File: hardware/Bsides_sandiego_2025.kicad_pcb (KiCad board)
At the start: 2 copper layers, 49.9 x 49.1 mm, 24 parts, among them J1 Conn_02x03_Odd_Even, SW1 RESET, SW2 SW_SPDT, U1 CH32V003FxPx

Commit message: feat(Hw):Update_PCB_And_Floorplan
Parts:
- added C3: 0.1uF, Capacitor_SMD:C_0603_1608Metric, F.Cu at (110.1, 115.6)
- added C4: 0.1uF, Capacitor_SMD:C_0603_1608Metric, F.Cu at (148.2, 115.8)
- added C5: 0.1uF, Capacitor_SMD:C_0603_1608Metric, F.Cu at (122.7, 115.6)
- added C6: 0.1uF, Capacitor_SMD:C_0603_1608Metric, F.Cu at (135.6, 115.7)
- added J2: OLED, Footprints:Display OLED 128 x32, F.Cu at (107.5, 100.1)
- added SW3: ~, Button_Switch_SMD:SW_SPST_TL3342, F.Cu at (105.1, 115.7)
- added SW4: ~, Button_Switch_SMD:SW_SPST_TL3342, F.Cu at (143.2, 115.8)
- added SW5: ~, Button_Switch_SMD:SW_SPST_TL3342, F.Cu at (117.7, 115.5)
- added SW6: ~, Button_Switch_SMD:SW_SPST_TL3342, F.Cu at (130.6, 115.7)
- moved R4 32.2 mm to (146.4, 77.6), turned to -90 degrees
- moved C2 25.5 mm to (105.3, 95.1), turned to 0 degrees
- moved R3 22.1 mm to (123.3, 60.5), turned to -90 degrees
- moved R6 19.5 mm to (116.9, 93.5)
- moved R7 17.2 mm to (135.2, 93.2)
- moved R1 14.3 mm to (113.5, 63.6), turned to 90 degrees
- moved R2 12.9 mm to (119.6, 67.5)
- moved R5 8.95 mm to (108.0, 77.6), turned to -90 degrees
- moved R8 5.18 mm to (131.8, 78.7)
- moved SW1 2.96 mm to (105.3, 91.4)
- moved C1 0.50 mm to (126.7, 83.2)
- turned D3 to -90 degrees
- turned D5 to -173.5 degrees
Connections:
- D1 pad 2: unconnected-(D1-A-Pad2) -> /LED1
- D2 pad 2: unconnected-(D2-A-Pad2) -> /LED2
- D3 pad 2: unconnected-(D3-A-Pad2) -> /LED3
- D4 pad 2: unconnected-(D4-A-Pad2) -> /LED4
- D5 pad 2: unconnected-(D5-A-Pad2) -> /LED5
- D6 pad 2: unconnected-(D6-A-Pad2) -> /LED6
- D7 pad 2: unconnected-(D7-A-Pad2) -> /LED7
- D8 pad 2: unconnected-(D8-A-Pad2) -> /LED8
- U1 pad 1: unconnected-(U1-PD4-Pad1) -> /LED1
- U1 pad 10: unconnected-(U1-PC0-Pad10) -> /LED7
- U1 pad 13: unconnected-(U1-PC3-Pad13) -> /LED8
- U1 pad 14: unconnected-(U1-PC4-Pad14) -> /LEFT
- U1 pad 15: unconnected-(U1-PC5-Pad15) -> /UP
- U1 pad 19: unconnected-(U1-PD2-Pad19) -> /DOWN
- U1 pad 2: unconnected-(U1-PD5-Pad2) -> /LED2
- U1 pad 20: unconnected-(U1-PD3-Pad20) -> /RIGHT
- U1 pad 3: unconnected-(U1-PD6-Pad3) -> /LED3
- U1 pad 5: unconnected-(U1-PA1-Pad5) -> /LED4
- U1 pad 6: unconnected-(U1-PA2-Pad6) -> /LED5
- U1 pad 8: unconnected-(U1-PD0-Pad8) -> /LED6
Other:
- board size 49.9 x 49.1 mm -> 49.9 x 71.1 mm

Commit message: feat(Hw):Update_Route
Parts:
- moved J1 78.9 mm to (67.1, 111.0)
- moved BT1 50.0 mm to (103.3, 103.6), turned to 90 degrees
- moved C4 47.4 mm to (101.0, 112.1)
- moved C6 47.1 mm to (88.5, 112.1)
- moved J2 38.9 mm to (68.8, 95.8)
- moved R8 38.8 mm to (93.3, 74.9)
- moved D1 38.3 mm to (75.3, 63.1)
- moved D3 38.3 mm to (90.3, 57.4)
- moved D7 38.3 mm to (95.4, 86.7)
- moved R1 38.3 mm to (75.3, 60.6)
- moved R2 38.3 mm to (81.4, 64.5)
- moved R7 38.3 mm to (97.1, 90.1)
- moved Ref** 38.3 mm to (86.6, 70.8)
- moved SW2 38.3 mm to (64.0, 76.8)
- moved U1 38.3 mm to (82.7, 77.8)
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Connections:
- C1 pad 2: VCC -> +3.3V
- J2 pad 3: VCC -> +3.3V
- U1 pad 1: /LED1 -> /LED3
- U1 pad 13: /LED8 -> /LEFT
- U1 pad 14: /LEFT -> /UP
- U1 pad 15: /UP -> /LED6
- U1 pad 19: /DOWN -> /LED5
- U1 pad 20: /RIGHT -> /LED1
- U1 pad 3: /LED3 -> /LED8
- U1 pad 6: /LED5 -> /DOWN
- U1 pad 8: /LED6 -> /RIGHT
- U1 pad 9: VCC -> +3.3V
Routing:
- net +3.3V: track 0.00 -> 109.1 mm, vias 0 -> 1
- net Net-(BT1--): track 0.00 -> 63.5 mm, vias 0 -> 2
- net /RIGHT: track 0.00 -> 62.0 mm, vias 0 -> 1
- net /LEFT: track 0.00 -> 56.7 mm, vias 0 -> 1
- net /SWDIO: track 0.00 -> 52.3 mm
- net /DOWN: track 0.00 -> 51.5 mm, vias 0 -> 1
- net /UP: track 0.00 -> 46.1 mm, vias 0 -> 1
- net /RST: track 0.00 -> 43.5 mm, vias 0 -> 2
- net /SCL: track 0.00 -> 32.1 mm
- net /SDA: track 0.00 -> 27.9 mm
- net /LED3: track 0.00 -> 21.0 mm, vias 0 -> 1
- net /LED4: track 0.00 -> 19.9 mm, vias 0 -> 1
- net /LED1: track 0.00 -> 15.3 mm, vias 0 -> 1
- net /LED8: track 0.00 -> 13.2 mm, vias 0 -> 1
- net /LED6: track 0.00 -> 13.1 mm
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- added copper zone on B.Cu, net GND
- added copper zone on F.Cu, net GND

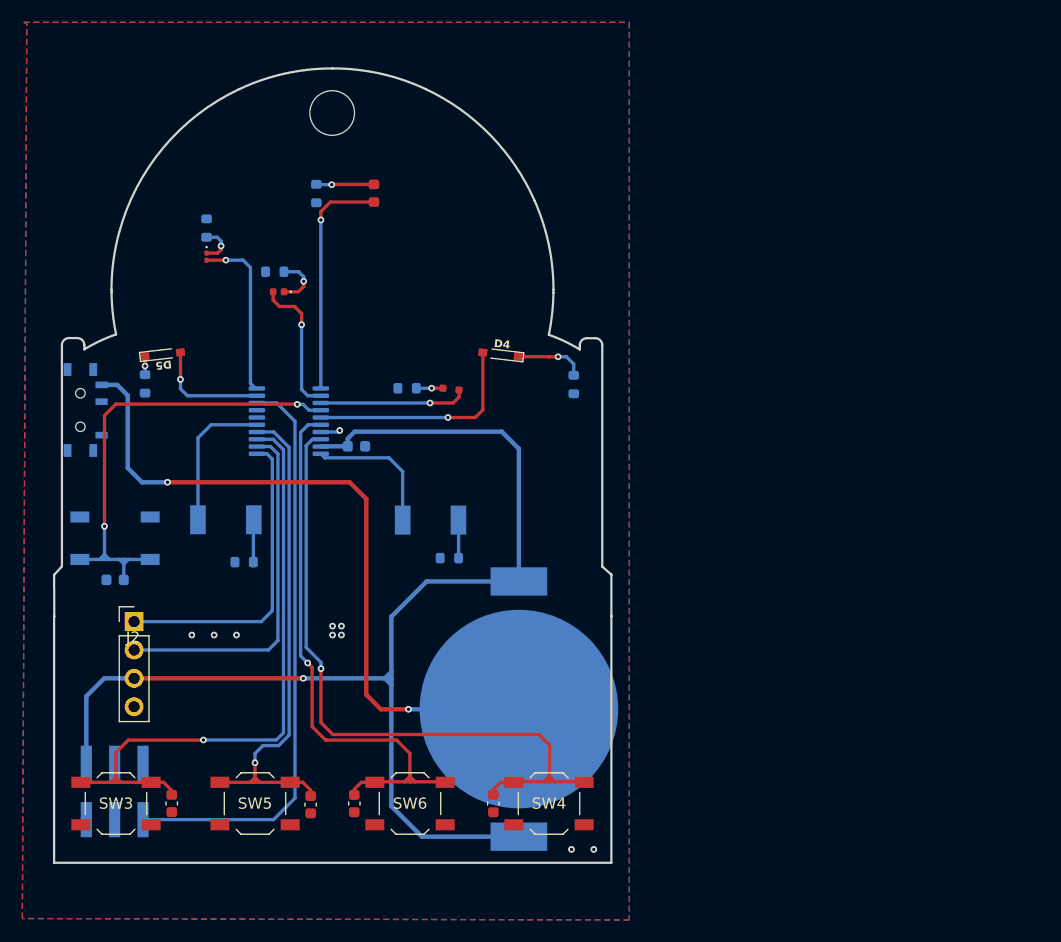
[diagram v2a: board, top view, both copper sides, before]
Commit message: feat(Hw):Update_Batt_Holder
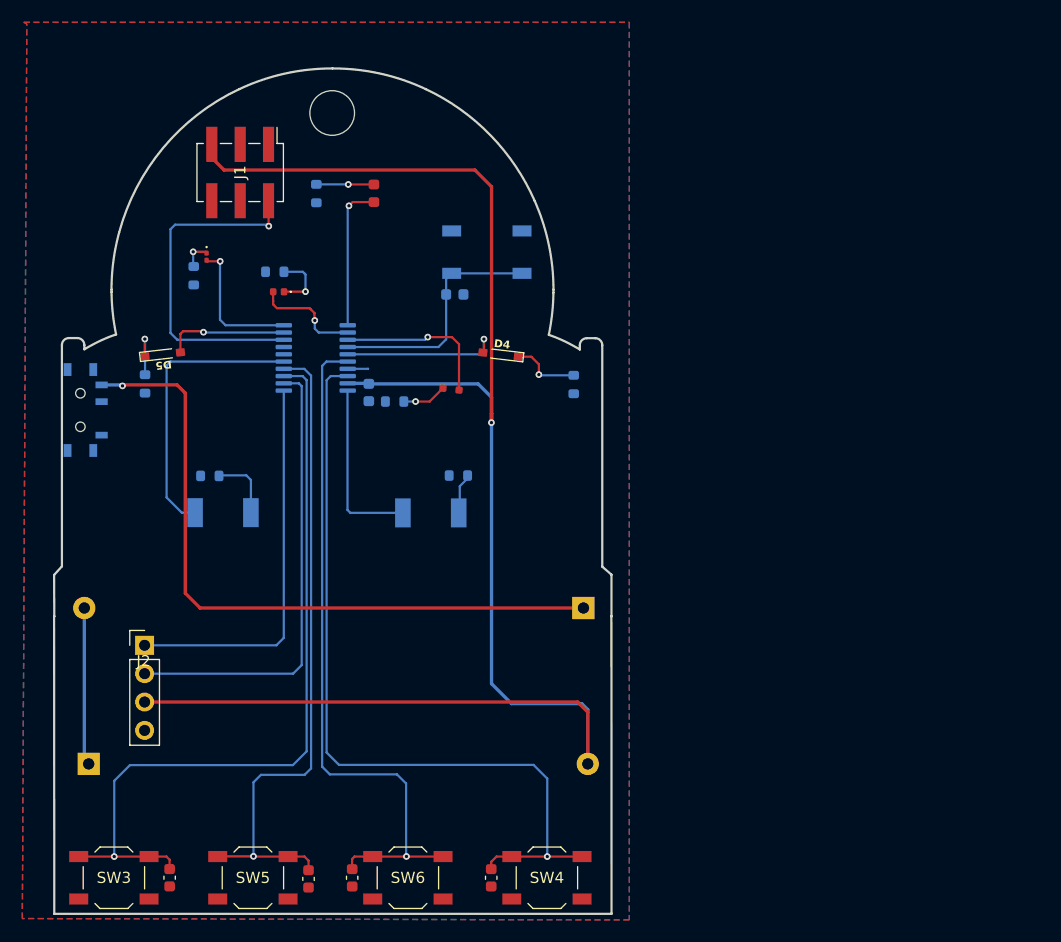
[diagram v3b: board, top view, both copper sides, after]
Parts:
- added BT2: Battery_Cell, Battery:BatteryHolder_Keystone_2466_1xAAA, B.Cu at (64.8, 108.5)
- BT1: footprint Batteries:BAT-HLD-001 -> Battery:BatteryHolder_Keystone_2466_1xAAA
- J1: moved to F.Cu
- moved J1 56.6 mm to (78.3, 55.6), turned to -90 degrees
- moved SW1 42.0 mm to (100.4, 62.7)
- moved C2 39.7 mm to (97.5, 66.5), turned to 180 degrees
- moved BT1 10.7 mm to (109.1, 94.6), turned to 180 degrees
- moved R6 8.31 mm to (75.6, 82.8)
- moved R7 7.43 mm to (97.9, 82.7)
- moved C3 6.65 mm to (72.0, 118.7)
- moved C5 6.65 mm to (84.5, 118.8)
- moved C4 6.65 mm to (100.8, 118.7)
- moved C6 6.65 mm to (88.4, 118.7)
- moved SW3 6.65 mm to (67.0, 118.7)
- moved SW4 6.65 mm to (105.8, 118.7)
- moved SW5 6.65 mm to (79.5, 118.7)
- moved SW6 6.65 mm to (93.3, 118.7)
- moved U1 6.15 mm to (85.1, 72.2)
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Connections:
- BT1 pad 2: +3.3V -> Net-(BT1-+)
- J1 pad 1: /SWDIO -> unconnected-(J1-Pin_1-Pad1)
- J1 pad 2: unconnected-(J1-Pin_2-Pad2) -> /SWDIO
- J1 pad 5: GND -> +3.3V
- J1 pad 6: +3.3V -> GND
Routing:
- net +3.3V: track 109.1 -> 147.5 mm
- net /RST: track 43.5 -> 21.5 mm, vias 2 -> 0
- net /SWDIO: track 52.3 -> 31.0 mm, vias 0 -> 1
- net Net-(BT1-+): track 0.00 -> 14.1 mm
- net /UP: track 46.1 -> 59.3 mm
- net /LEFT: track 56.7 -> 69.6 mm
- net /LED6: track 13.1 -> 25.6 mm
- net /DOWN: track 51.5 -> 62.2 mm
- net /RIGHT: track 62.0 -> 72.1 mm
- net /SCL: track 32.1 -> 41.1 mm
- net /LED3: track 21.0 -> 13.1 mm
- net /SDA: track 27.9 -> 34.9 mm
- net /LED4: track 19.9 -> 14.6 mm
- net /LED7: track 12.3 -> 15.8 mm
- net Net-(D5-K): track 1.64 -> 4.77 mm
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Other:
- board size 49.9 x 71.1 mm -> 49.9 x 75.7 mm

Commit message: feat(Hw):Update_csv_And_Size
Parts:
- added kibuzzard-67607E30: G***, kibuzzard-67607E30, B.Cu at (64.5, 86.5)
- added kibuzzard-67607E30: G***, kibuzzard-67607E30, B.Cu at (110.7, 116.3)
- moved C5 4.57 mm to (84.4, 114.3)
- moved C3 4.57 mm to (72.0, 114.2)
- moved C4 4.57 mm to (100.8, 114.2)
- moved C6 4.57 mm to (88.3, 114.2)
- moved SW3 4.57 mm to (67.0, 114.2)
- moved SW4 4.57 mm to (105.8, 114.2)
- moved SW5 4.57 mm to (79.4, 114.2)
- moved SW6 4.57 mm to (93.3, 114.2)
- moved BT1 0.22 mm to (109.3, 94.5)
- moved BT2 0.16 mm to (64.6, 108.6)
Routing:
- net /UP: track 59.3 -> 55.1 mm
- net /DOWN: track 62.2 -> 58.0 mm
- net /RIGHT: track 72.1 -> 68.0 mm
- net /LEFT: track 69.6 -> 65.6 mm
- net +3.3V: track 147.5 -> 148.2 mm
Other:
- board size 49.9 x 75.7 mm -> 49.9 x 71.2 mm

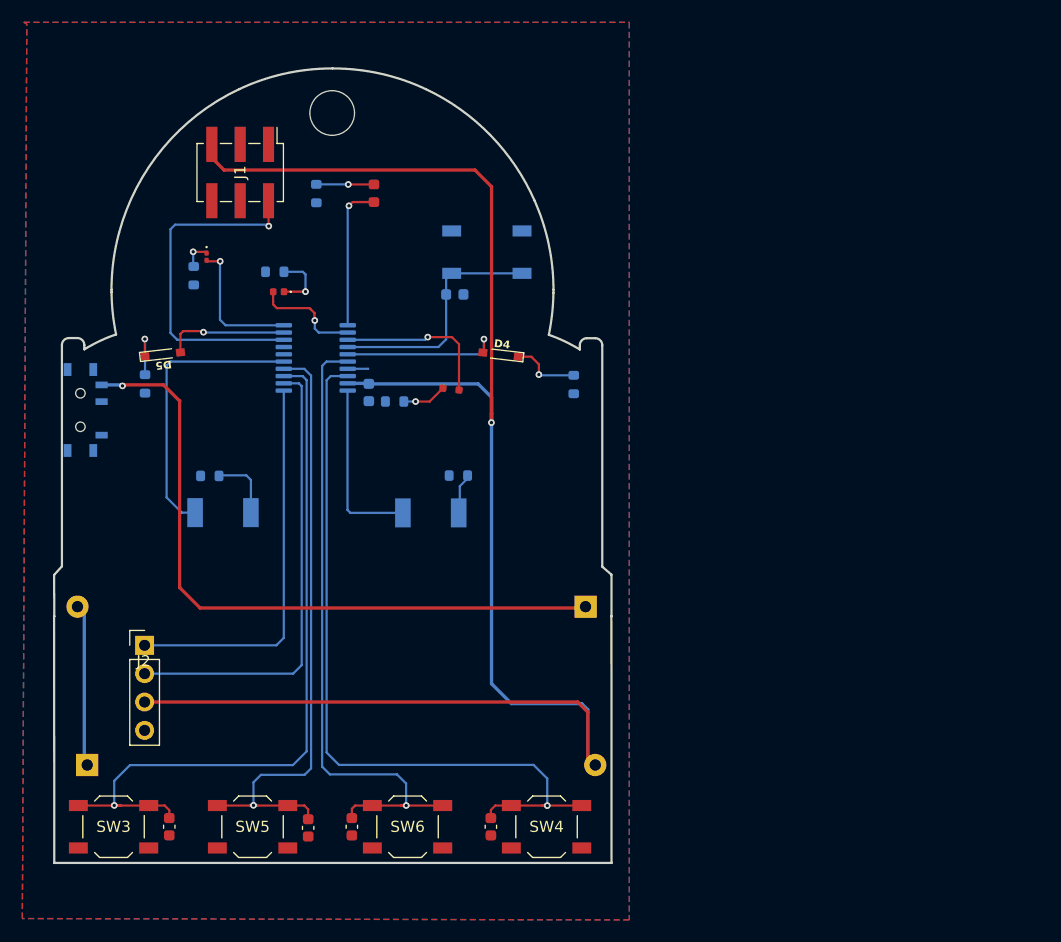
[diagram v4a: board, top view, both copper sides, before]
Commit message: feat(Hw):Update_Add_On_Connector
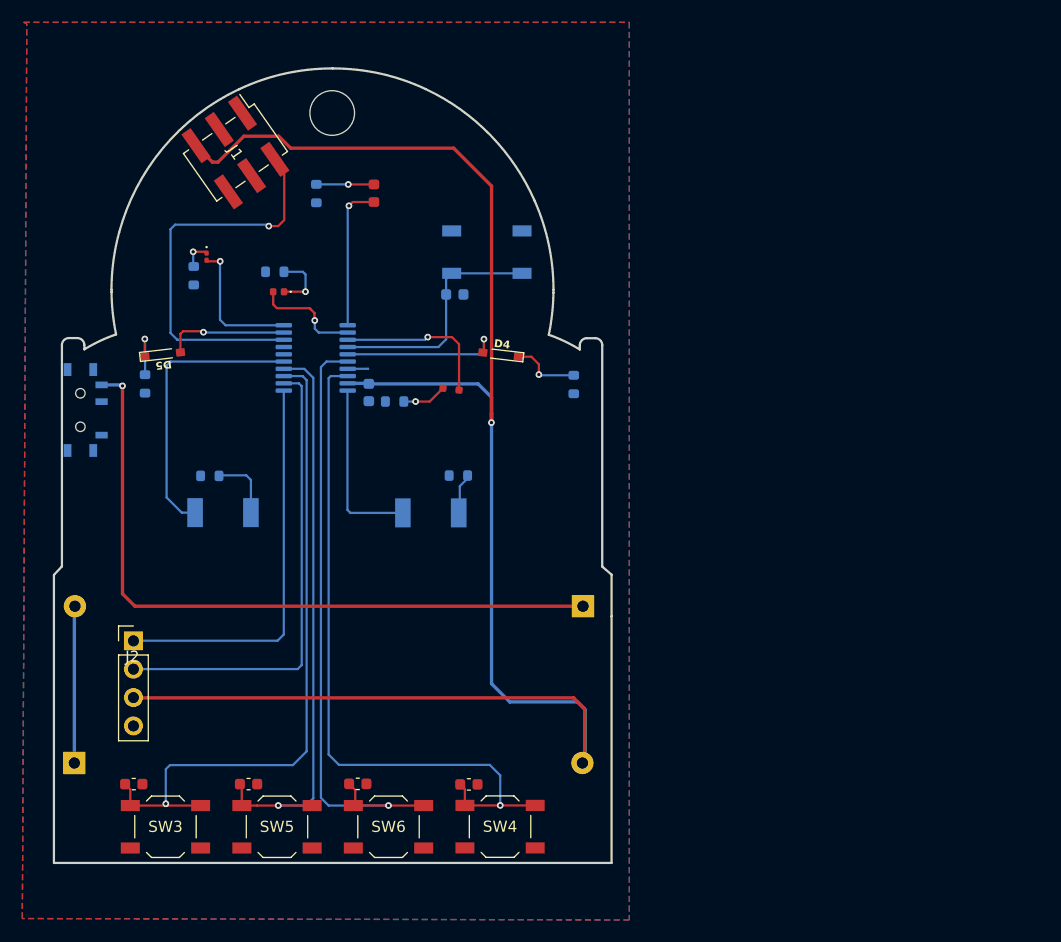
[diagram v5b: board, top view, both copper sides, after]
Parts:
- moved C5 6.62 mm to (79.1, 110.3), turned to 180 degrees
- moved C3 4.97 mm to (68.8, 110.3), turned to 180 degrees
- moved SW3 4.65 mm to (71.6, 114.2)
- moved C4 4.27 mm to (98.8, 110.4), turned to 180 degrees
- moved SW4 4.17 mm to (101.6, 114.2)
- moved C6 3.88 mm to (88.9, 110.3), turned to 180 degrees
- moved SW5 2.19 mm to (81.6, 114.2)
- moved J1 1.84 mm to (77.9, 53.8), turned to -55 degrees
- moved SW6 1.71 mm to (91.6, 114.2)
- moved BT2 1.16 mm to (63.5, 108.5)
- moved J2 1.08 mm to (68.8, 97.5)
- moved BT1 0.23 mm to (109.0, 94.4)
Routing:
- net /RIGHT: track 68.0 -> 62.7 mm
- net /LEFT: track 65.6 -> 60.4 mm
- net /SWDIO: track 31.0 -> 36.1 mm
- net /UP: track 55.1 -> 52.1 mm
- net +3.3V: track 148.2 -> 150.8 mm
- net /DOWN: track 58.0 -> 56.0 mm
- net /SCL: track 41.1 -> 41.9 mm
- net Net-(BT1--): track 61.5 -> 62.2 mm
- net /SDA: track 34.9 -> 35.5 mm
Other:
- outline, holes or cut-outs redrawn
